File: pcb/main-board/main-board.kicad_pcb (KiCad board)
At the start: 2 copper layers, 48.8 x 57.2 mm, 3 parts, among them U1 PicoW

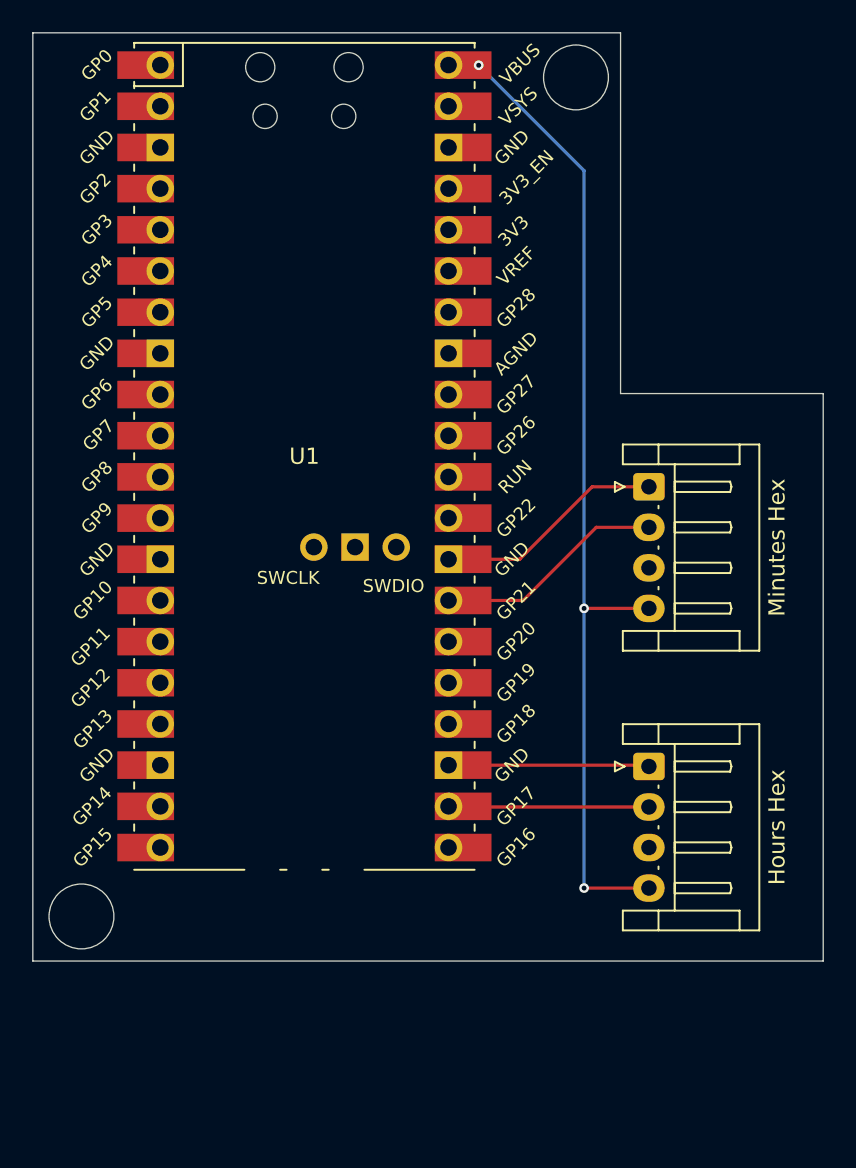
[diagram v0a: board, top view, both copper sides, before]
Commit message: Added switch
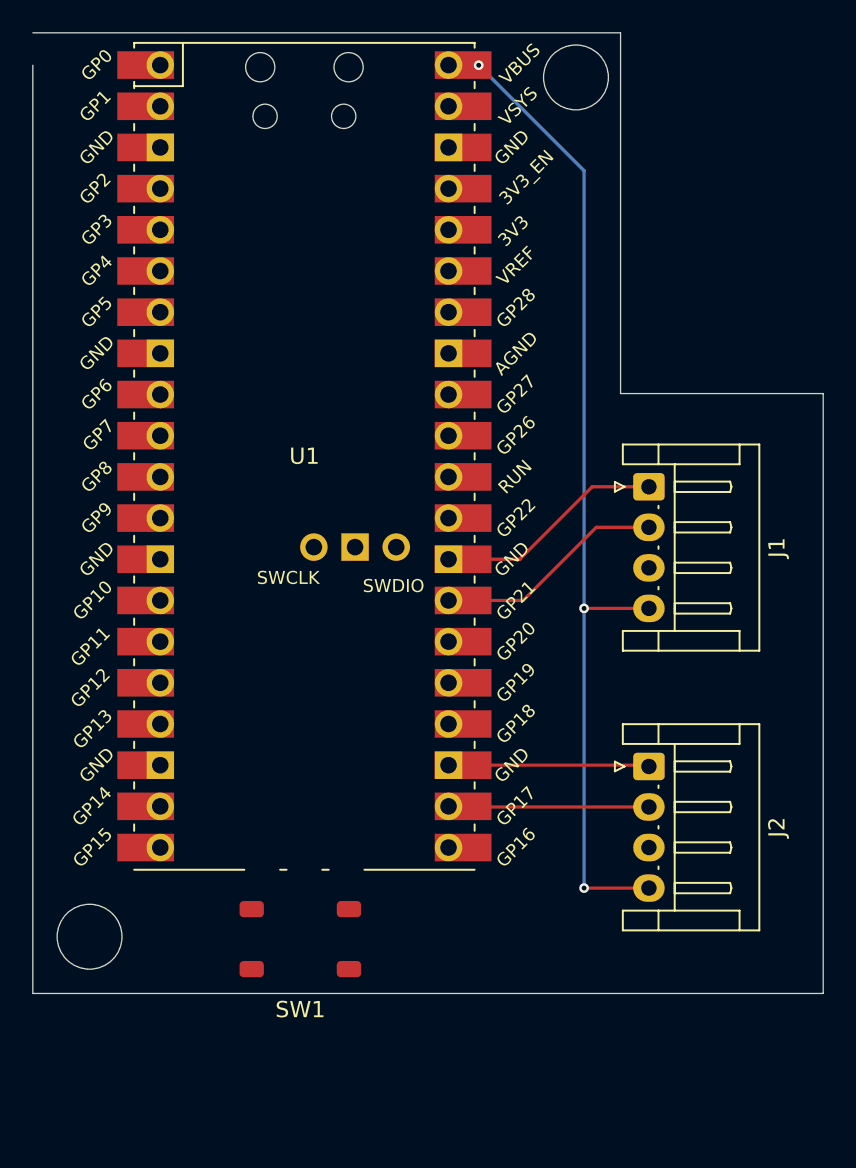
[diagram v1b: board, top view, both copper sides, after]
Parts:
- added SW1: SW_Push, RaspberryPI PicoW:Switch, F.Cu at (146.5, 124.5)
- J1: renamed from Minutes Hex
- J2: renamed from Hours Hex
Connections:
- U1 pad 18: unconnected-(U1-GND-Pad18) -> Net-(SW1-Pad2)
- U1 pad 20: unconnected-(U1-GPIO15-Pad20)_0 -> Net-(U1-GPIO15)
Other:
- board size 48.8 x 57.2 mm -> 48.8 x 59.2 mm
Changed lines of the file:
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@@
 	(net 4 "Net-(J2-Pin_1)")
 	(net 5 "Net-(J2-Pin_2)")
-	(net 6 "unconnected-(U1-GPIO15-Pad20)")
+	(net 6 "Net-(U1-GPIO15)")
 	(net 7 "unconnected-(U1-GND-Pad42)")
 	(net 8 "unconnected-(U1-3V3_EN-Pad37)")
@@
 	(net 27 "unconnected-(U1-GPIO27_ADC1-Pad32)_0")
 	(net 28 "unconnected-(U1-GPIO2-Pad4)_0")
-	(net 29 "unconnected-(U1-GPIO15-Pad20)_0")
+	(net 29 "Net-(SW1-Pad2)")
 	(net 30 "unconnected-(U1-GPIO9-Pad12)")
 	(net 31 "unconnected-(U1-3V3-Pad36)")
@@
 	(net 76 "Net-(J1-Pin_2)")
 	(net 77 "unconnected-(U1-GPIO10-Pad14)")
-	(net 78 "unconnected-(U1-GND-Pad18)")
 	(footprint "RaspberryPI PicoW:RPi_PicoW_SMD_TH"
 		(layer "F.Cu")
@@
 			(layers "*.Cu" "*.Mask")
 			(remove_unused_layers no)
-			(net 78 "unconnected-(U1-GND-Pad18)")
+			(net 29 "Net-(SW1-Pad2)")
 			(pinfunction "GND")
 			(pintype "power_in")
@@
 			)
 			(layers "F.Cu" "F.Mask")
-			(net 78 "unconnected-(U1-GND-Pad18)")
+			(net 29 "Net-(SW1-Pad2)")
 			(pinfunction "GND")
 			(pintype "power_in")
@@
 			(layers "*.Cu" "*.Mask")
 			(remove_unused_layers no)
-			(net 6 "unconnected-(U1-GPIO15-Pad20)")
+			(net 6 "Net-(U1-GPIO15)")
 			(pinfunction "GPIO15")
-			(pintype "bidirectional+no_connect")
+			(pintype "bidirectional")
 		)
 		(pad "20" smd rect
@@
 			)
 			(layers "F.Cu" "F.Mask")
-			(net 29 "unconnected-(U1-GPIO15-Pad20)_0")
+			(net 6 "Net-(U1-GPIO15)")
 			(pinfunction "GPIO15")
-			(pintype "bidirectional+no_connect")
+			(pintype "bidirectional")
 		)
 		(pad "21" thru_hole oval
@@
 		(descr "JST EH series connector, S4B-EH (http://www.jst-mfg.com/product/pdf/eng/eEH.pdf), generated with kicad-footprint-generator")
 		(tags "connector JST EH horizontal")
-		(property "Reference" "Minutes Hex"
+		(property "Reference" "J1"
 			(at 3.75 -7.9 90)
 			(layer "F.SilkS")
@@
 		(descr "JST EH series connector, S4B-EH (http://www.jst-mfg.com/product/pdf/eng/eEH.pdf), generated with kicad-footprint-generator")
 		(tags "connector JST EH horizontal")
-		(property "Reference" "Hours Hex"
+		(property "Reference" "J2"
 			(at 3.75 -7.9 90)
 			(layer "F.SilkS")
@@
 		)
 	)
+	(footprint "RaspberryPI PicoW:Switch"
+		(layer "F.Cu")
+		(at 146.5 124.5)
+		(property "Reference" "SW1"
+			(at 0 -0.5 0)
+			(unlocked yes)
+			(layer "F.SilkS")
+			(effects
+				(font
+					(size 1 1)
+					(thickness 0.1)
+				)
+			)
+		)
+		(property "Value" "SW_Push"
+			(at 0 1 0)
+			(unlocked yes)
+			(layer "F.Fab")
+			(effects
+				(font
+					(size 1 1)
+					(thickness 0.15)
+				)
+			)
+		)
+		(property "Footprint" "RaspberryPI PicoW:Switch"
+			(at 0 0 0)
+			(unlocked yes)
+			(layer "F.Fab")
+			(hide yes)
+			(effects
+				(font
+					(size 1 1)
+					(thickness 0.15)
+				)
+			)
+		)
+		(property "Datasheet" ""
+			(at 0 0 0)
+			(unlocked yes)
+			(layer "F.Fab")
+			(hide yes)
+			(effects
+				(font
+					(size 1 1)
+					(thickness 0.15)
+				)
+			)
+		)
+		(property "Description" "Push button switch, generic, two pins"
+			(at 0 0 0)
+			(unlocked yes)
+			(layer "F.Fab")
+			(hide yes)
+			(effects
+				(font
+					(size 1 1)
+					(thickness 0.15)
+				)
+			)
+		)
+		(sheetname "Root")
+		(sheetfile "main-board.kicad_sch")
+		(attr smd)
+		(fp_text user "${REFERENCE}"
+			(at 0 2.5 0)
+			(unlocked yes)
+			(layer "F.Fab")
+			(effects
+				(font
+					(size 1 1)
+					(thickness 0.15)
+				)
+			)
+		)
+		(pad "1" smd roundrect
+			(at -3 -6.7)
+			(size 1.5 1)
+			(layers "F.Cu" "F.Paste" "F.Mask")
+			(roundrect_rratio 0.25)
+			(net 6 "Net-(U1-GPIO15)")
+			(pinfunction "1")
+			(pintype "passive")
+			(thermal_bridge_angle 45)
+		)
+		(pad "1" smd roundrect
+			(at 3 -6.7)
+			(size 1.5 1)
+			(layers "F.Cu" "F.Paste" "F.Mask")
+			(roundrect_rratio 0.25)
+			(net 6 "Net-(U1-GPIO15)")
+			(pinfunction "1")
+			(pintype "passive")
+			(thermal_bridge_angle 45)
+		)
+		(pad "2" smd roundrect
+			(at -3 -3)
+			(size 1.5 1)
+			(layers "F.Cu" "F.Paste" "F.Mask")
+			(roundrect_rratio 0.25)
+			(net 29 "Net-(SW1-Pad2)")
+			(pinfunction "2")
+			(pintype "passive")
+			(thermal_bridge_angle 45)
+		)
+		(pad "2" smd roundrect
+			(at 3 -3)
+			(size 1.5 1)
+			(layers "F.Cu" "F.Paste" "F.Mask")
+			(roundrect_rratio 0.25)
+			(net 29 "Net-(SW1-Pad2)")
+			(pinfunction "2")
+			(pintype "passive")
+			(thermal_bridge_angle 45)
+		)
+	)
 	(gr_line
 		(start 130 63.75)
@@
 	)
 	(gr_line
-		(start 178.75 121)
-		(end 130 121)
+		(start 178.75 123)
+		(end 130 123)
 		(stroke
 			(width 0.05)
@@
 	(gr_line
 		(start 178.75 86)
-		(end 178.75 121)
+		(end 178.75 123)
 		(stroke
 			(width 0.05)
@@
 	)
 	(gr_circle
-		(center 133 118.25)
-		(end 135 118.25)
+		(center 133.5 119.5)
+		(end 135.5 119.5)
 		(stroke
 			(width 0.05)
@@
 	)
 	(gr_line
-		(start 130 121)
-		(end 130 63.75)
+		(start 130 123)
+		(end 130 65.75)
 		(stroke
 			(width 0.05)

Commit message: Finished switch placement and wiring
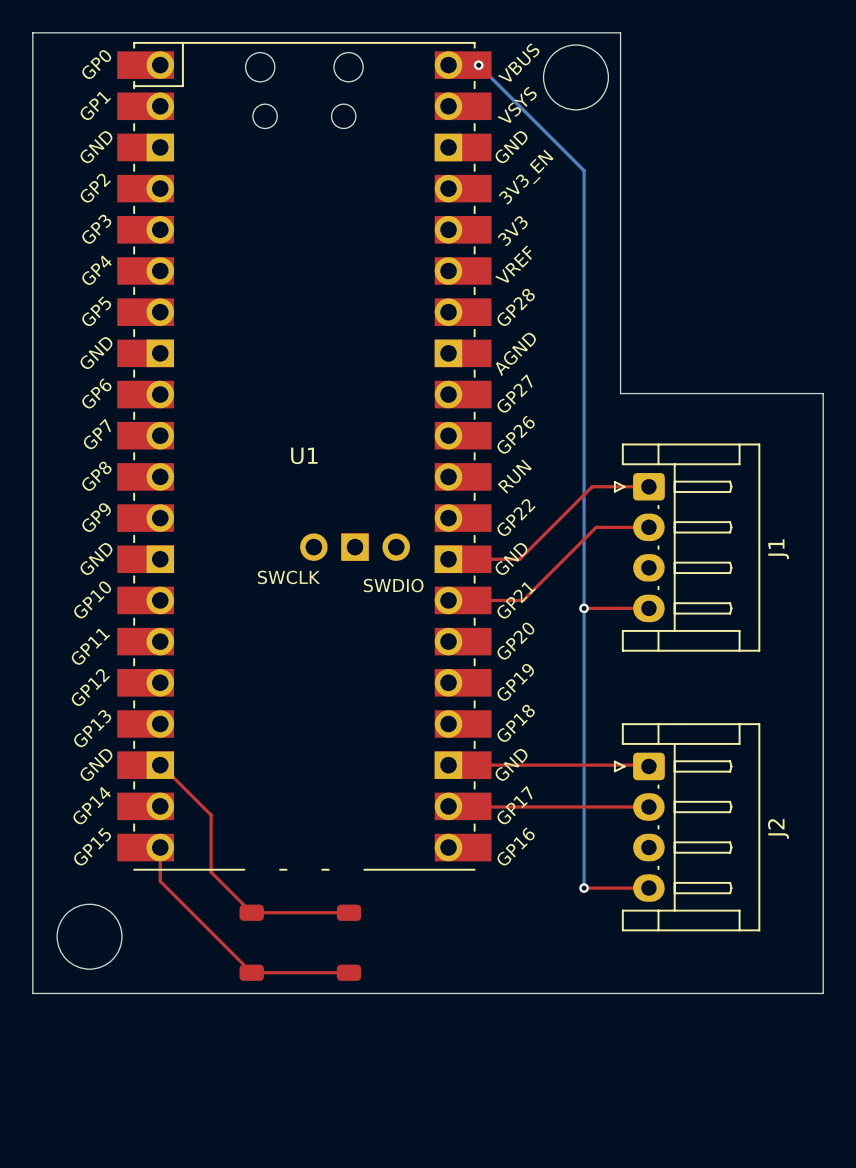
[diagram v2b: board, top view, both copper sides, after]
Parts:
- moved SW1 9.47 mm to (146.5, 115.0), turned to 180 degrees
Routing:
- net Net-(SW1-Pad2): track 0.00 -> 17.5 mm
- net Net-(U1-GPIO15): track 0.00 -> 16.1 mm
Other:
- outline, holes or cut-outs redrawn
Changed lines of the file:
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@@
 	(footprint "RaspberryPI PicoW:Switch"
 		(layer "F.Cu")
-		(at 146.5 124.5)
+		(at 146.5 115.025 180)
 		(property "Reference" "SW1"
-			(at 0 -0.5 0)
+			(at 0 -0.5 180)
 			(unlocked yes)
 			(layer "F.SilkS")
+			(hide yes)
 			(effects
 				(font
@@
 		)
 		(property "Value" "SW_Push"
-			(at 0 1 0)
+			(at 0 1 180)
 			(unlocked yes)
 			(layer "F.Fab")
+			(hide yes)
 			(effects
 				(font
@@
 		)
 		(property "Footprint" "RaspberryPI PicoW:Switch"
-			(at 0 0 0)
+			(at 0 0 180)
 			(unlocked yes)
 			(layer "F.Fab")
@@
 		)
 		(property "Datasheet" ""
-			(at 0 0 0)
+			(at 0 0 180)
 			(unlocked yes)
 			(layer "F.Fab")
@@
 		)
 		(property "Description" "Push button switch, generic, two pins"
-			(at 0 0 0)
+			(at 0 0 180)
 			(unlocked yes)
 			(layer "F.Fab")
@@
 		(sheetfile "main-board.kicad_sch")
 		(attr smd)
-		(fp_text user "${REFERENCE}"
-			(at 0 2.5 0)
-			(unlocked yes)
-			(layer "F.Fab")
-			(effects
-				(font
-					(size 1 1)
-					(thickness 0.15)
-				)
-			)
-		)
 		(pad "1" smd roundrect
-			(at -3 -6.7)
+			(at -3 -6.7 180)
 			(size 1.5 1)
 			(layers "F.Cu" "F.Paste" "F.Mask")
@@
 		)
 		(pad "1" smd roundrect
-			(at 3 -6.7)
+			(at 3 -6.7 180)
 			(size 1.5 1)
 			(layers "F.Cu" "F.Paste" "F.Mask")
@@
 		)
 		(pad "2" smd roundrect
-			(at -3 -3)
+			(at -3 -3 180)
 			(size 1.5 1)
 			(layers "F.Cu" "F.Paste" "F.Mask")
@@
 		)
 		(pad "2" smd roundrect
-			(at 3 -3)
+			(at 3 -3 180)
 			(size 1.5 1)
 			(layers "F.Cu" "F.Paste" "F.Mask")
@@
 	(gr_line
 		(start 130 123)
-		(end 130 65.75)
+		(end 130 63.75)
 		(stroke
 			(width 0.05)
@@
 	)
 	(segment
+		(start 149.5 121.725)
+		(end 143.5 121.725)
+		(width 0.2)
+		(layer "F.Cu")
+		(net 6)
+	)
+	(segment
+		(start 137.86 116.085)
+		(end 137.86 114)
+		(width 0.2)
+		(layer "F.Cu")
+		(net 6)
+	)
+	(segment
+		(start 143.5 121.725)
+		(end 137.86 116.085)
+		(width 0.2)
+		(layer "F.Cu")
+		(net 6)
+	)
+	(segment
+		(start 143.5 118.025)
+		(end 141 115.525)
+		(width 0.2)
+		(layer "F.Cu")
+		(net 29)
+	)
+	(segment
+		(start 141 112)
+		(end 137.92 108.92)
+		(width 0.2)
+		(layer "F.Cu")
+		(net 29)
+	)
+	(segment
+		(start 143.5 118.025)
+		(end 149.5 118.025)
+		(width 0.2)
+		(layer "F.Cu")
+		(net 29)
+	)
+	(segment
+		(start 141 115.525)
+		(end 141 112)
+		(width 0.2)
+		(layer "F.Cu")
+		(net 29)
+	)
+	(segment
+		(start 137.92 108.92)
+		(end 137.86 108.92)
+		(width 0.2)
+		(layer "F.Cu")
+		(net 29)
+	)
+	(segment

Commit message: Added JST connector to hex board
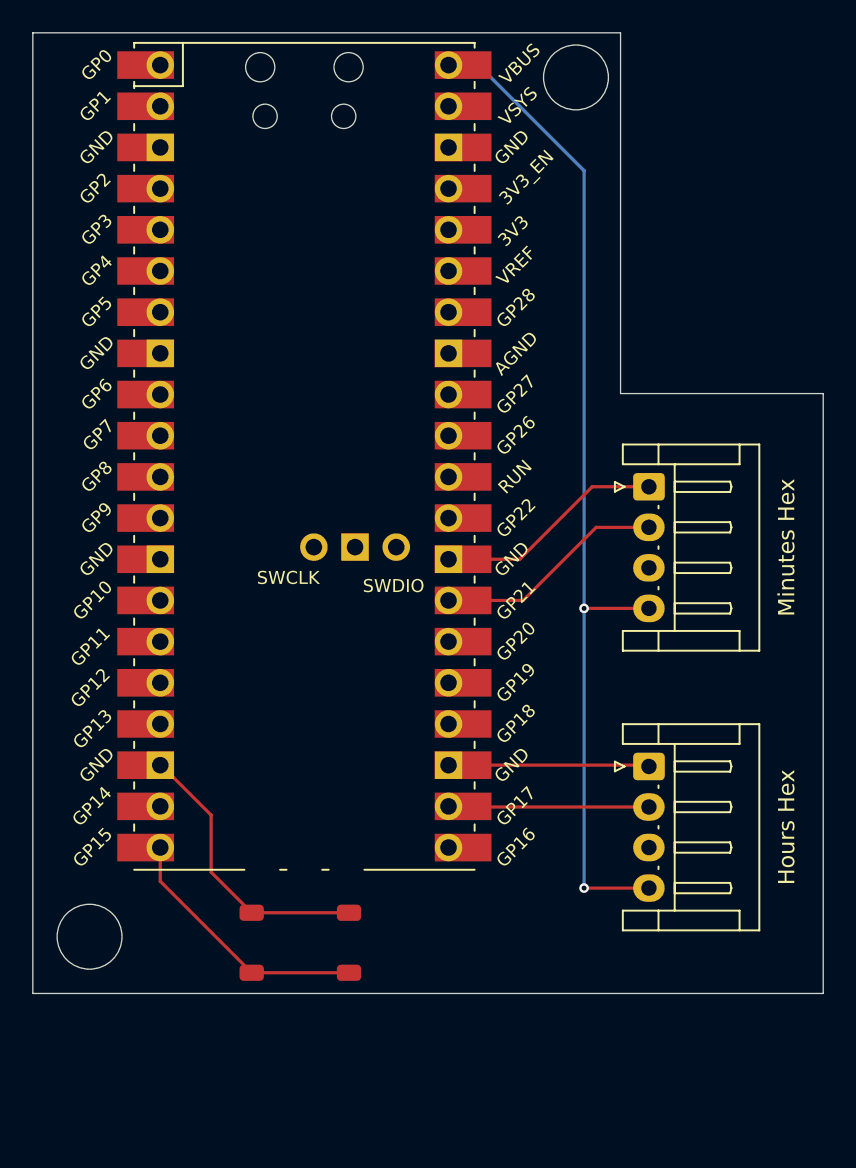
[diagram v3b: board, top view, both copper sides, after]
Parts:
- Hours Hex: renamed from J2
- Minutes Hex: renamed from J1
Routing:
- net Net-(J1-Pin_4): track 61.4 -> 63.3 mm, vias 3 -> 2
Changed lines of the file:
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@@
 			(at 0 0 0)
 			(layer "F.SilkS")
+			(hide yes)
 			(effects
 				(font
@@
 		(descr "JST EH series connector, S4B-EH (http://www.jst-mfg.com/product/pdf/eng/eEH.pdf), generated with kicad-footprint-generator")
 		(tags "connector JST EH horizontal")
-		(property "Reference" "J1"
-			(at 3.75 -7.9 90)
+		(property "Reference" "Minutes Hex"
+			(at 3.75 -8.5 90)
 			(layer "F.SilkS")
 			(effects
@@
 		(descr "JST EH series connector, S4B-EH (http://www.jst-mfg.com/product/pdf/eng/eEH.pdf), generated with kicad-footprint-generator")
 		(tags "connector JST EH horizontal")
-		(property "Reference" "J2"
-			(at 3.75 -7.9 90)
+		(property "Reference" "Hours Hex"
+			(at 3.75 -8.5 90)
 			(layer "F.SilkS")
 			(effects
@@
 	)
 	(via
-		(at 157.5 65.75)
-		(size 0.6)
-		(drill 0.3)
-		(layers "F.Cu" "B.Cu")
-		(net 2)
-	)
-	(via
 		(at 164 116.5)
 		(size 0.6)
@@
 	)
 	(segment
-		(start 164 72.25)
-		(end 157.5 65.75)
+		(start 157.49 65.74)
+		(end 164 72.25)
 		(width 0.2)
 		(layer "B.Cu")
@@
 	)
 	(segment
-		(start 164 99.25)
-		(end 164 72.25)
+		(start 155.64 65.74)
+		(end 157.49 65.74)
 		(width 0.2)
 		(layer "B.Cu")
@@
 		(end 164 99.25)
 		(width 0.2)
+		(layer "B.Cu")
+		(net 2)
+	)
+	(segment
+		(start 164 72.25)
+		(end 164 99.25)
+		(width 0.2)

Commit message: Added colon LEDs, moved stuff around the board, etc
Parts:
- added LED1: LED_SK6812RGBW_5050Metric_Pad1.5x1.5mm_HandSolder, RaspberryPI PicoW:LED_SK6812RGBW_5050Metric_Pad1.5x1.5mm_HandSolder, B.Cu at (172.7, 126.5)
- added LED2: LED_SK6812RGBW_5050Metric_Pad1.5x1.5mm_HandSolder, RaspberryPI PicoW:LED_SK6812RGBW_5050Metric_Pad1.5x1.5mm_HandSolder, B.Cu at (153.8, 126.5)
- J1: renamed from Minutes Hex
- J2: renamed from Hours Hex
- moved J1 15.8 mm to (168.7, 76.0)
- moved J2 15.8 mm to (168.7, 93.2)
- moved SW1 7.10 mm to (144.2, 121.8), turned to 90 degrees
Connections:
- U1 pad 21: unconnected-(U1-GPIO16-Pad21) -> Net-(LED1-Data_IN)
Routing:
- net Net-(J2-Pin_1): track 12.4 -> 59.6 mm, vias 0 -> 1
- net Net-(J1-Pin_4): track 63.3 -> 99.5 mm
- net Net-(LED1-Data_IN): track 0.00 -> 21.3 mm, vias 0 -> 1
- net Net-(LED1-Data_OUT): track 0.00 -> 16.4 mm
- net Net-(J1-Pin_2): track 14.2 -> 27.5 mm
- net Net-(J1-Pin_1): track 14.2 -> 27.2 mm
- net Net-(J2-Pin_2): track 12.4 -> 23.3 mm
- net Net-(U1-GPIO15): track 16.1 -> 10.8 mm
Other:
- board size 48.8 x 59.2 mm -> 48.8 x 68 mm
